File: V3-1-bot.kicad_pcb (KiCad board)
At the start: 4 copper layers, 145 x 74.9 mm, 36 parts, among them IC1 MCP4451-103E_ST, IC2 MCP4451-103E_ST, IC3 MCP4451-103E_ST, J1 PowerPole, J2 Conn_01x12_Female, J3 Conn_01x12_Female, J4 Conn_01x03_Female, J5 Conn_01x03_Female, J6 Conn_01x03_Female, J7 Conn_01x03_Female, J8 Conn_01x03_Female, J9 Conn_01x03_Female, U1 Teensy4.0-Tall-Dog-Breakout, U2 AMPLIFIER-PAM8403, U3 AMPLIFIER-PAM8403, U4 AMPLIFIER-PAM8403, U5 AMPLIFIER-PAM8403, U6 AMPLIFIER-PAM8403, U7 AMPLIFIER-PAM8403

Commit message: Updated BOT
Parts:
- moved R1 112.8 mm to (38.6, 82.3), turned to 90 degrees
- moved R2 107.9 mm to (43.7, 82.3), turned to 90 degrees
- moved J2 95.4 mm to (35.3, 89.2), turned to 90 degrees
- moved J3 89.6 mm to (35.1, 96.3), turned to 90 degrees
- moved R12 25.1 mm to (105.4, 119.9)
- moved C1 17.6 mm to (43.2, 115.3)
- moved C2 17.2 mm to (124.5, 116.3)
- moved C3 17.0 mm to (83.6, 116.3)
- moved U1 16.6 mm to (89.7, 87.9)
- moved J4 16.3 mm to (165.9, 137.4)
- moved J5 15.3 mm to (108.7, 137.4)
- moved R9 15.1 mm to (139.2, 118.9), turned to 0 degrees
- moved R3 14.8 mm to (57.9, 119.1)
- moved J6 14.3 mm to (108.7, 107.4)
- moved J8 13.7 mm to (165.9, 107.4)
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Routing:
- net VDD: track 0.00 -> 273.9 mm
- net GND: track 0.00 -> 210.8 mm
- net SPEAK7-: track 0.00 -> 135.7 mm
- net SPEAK8-: track 0.00 -> 132.2 mm
- net SPEAK7+: track 0.00 -> 129.8 mm, vias 0 -> 1
- net SPEAK8+: track 0.00 -> 120.2 mm, vias 0 -> 1
- net SPEAK5-: track 0.00 -> 112.2 mm
- net SPEAK5+: track 0.00 -> 104.8 mm, vias 0 -> 1
- net SPEAK6+: track 0.00 -> 93.4 mm, vias 0 -> 1
- net SPEAK6-: track 0.00 -> 93.3 mm
- net SPEAK11-: track 0.00 -> 81.5 mm
- net SPEAK11+: track 0.00 -> 73.1 mm
- net SPEAK9-: track 0.00 -> 69.9 mm, vias 0 -> 1
- net FREQ14: track 0.00 -> 67.7 mm
- net SPEAK1-: track 0.00 -> 67.3 mm
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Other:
- board size 145 x 74.9 mm -> 145 x 71.4 mm

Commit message: Done BOT v3.1
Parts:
- added ?: , HART:hart-logo-2000-2000dpi, F.Cu at (41.7, 76.5)
- R1, R2: moved to B.Cu
- U1: footprint Teensy:TallDogTeensy4.0Breakout -> HART:TallDogTeensy4.0Breakout
- U2, U3, U4, U5, U6, U7: value AMPLIFIER-PAM8403 -> >VALUE
- moved R1 51.8 mm to (89.2, 93.8)
- moved R2 42.0 mm to (84.1, 93.8)
- moved R6 7.19 mm to (58.2, 123.4), turned to 0 degrees
- moved R3 6.12 mm to (51.8, 118.4), turned to 0 degrees
- moved R12 5.80 mm to (99.6, 120.1)
- moved R5 5.56 mm to (58.1, 118.4), turned to 0 degrees
- moved R4 2.36 mm to (51.8, 123.7), turned to 0 degrees
- moved R11 0.76 mm to (99.5, 123.3)
- moved R13 0.76 mm to (93.5, 123.3)
- moved R14 0.76 mm to (93.5, 119.9)
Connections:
- J5 pad 2: GND -> (no net)
- R6 pad 1: (no net) -> FREQ1
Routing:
- net FREQ4: track 0.00 -> 165.1 mm, vias 0 -> 2
- net FREQ2: track 0.00 -> 163.9 mm, vias 0 -> 2
- net TeensyVDD: track 54.9 -> 218.2 mm, vias 3 -> 10
- net FREQ3: track 0.00 -> 160.9 mm, vias 0 -> 2
- net FREQ10: track 0.00 -> 158.6 mm, vias 0 -> 1
- net FREQ1: track 0.00 -> 156.4 mm, vias 0 -> 2
- net FREQ9: track 0.00 -> 138.9 mm, vias 0 -> 2
- net SCL0: track 2.95 -> 122.7 mm, vias 1 -> 5
- net SDA0: track 2.08 -> 120.3 mm, vias 1 -> 5
- net FREQ8: track 0.00 -> 101.0 mm, vias 0 -> 2
- net FREQ13: track 0.00 -> 98.7 mm
- net FREQ6: track 1.80 -> 100.3 mm, vias 1 -> 2
- net GND: track 210.8 -> 308.8 mm
- net FREQ7: track 0.00 -> 92.2 mm, vias 0 -> 2
- net FREQ5: track 1.73 -> 89.4 mm, vias 1 -> 2
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- added copper zone on B.Cu, net GND
- added copper zone on F.Cu, net TeensyVDD
- added copper zone on F.Cu, net VDD
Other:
- outline, holes or cut-outs redrawn
- board text added: "GND"
- board text added: "HART Prototype V3.1"
- board text added: "VDD"
- board text added: "WARNING! DO NOT REVERSE POLARITY!!"

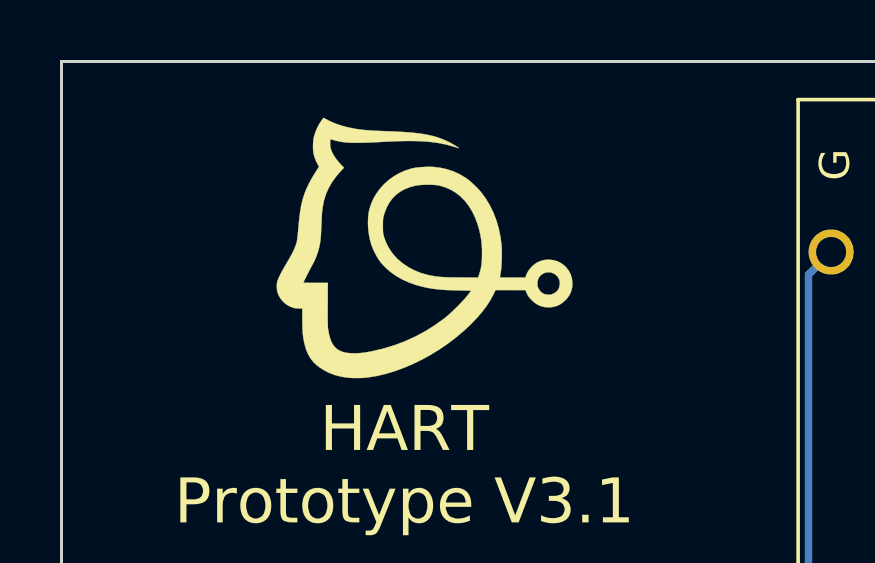
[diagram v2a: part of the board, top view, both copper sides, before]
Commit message: Cleanup symbols and libraries and add separate submodule for kicad-libaries
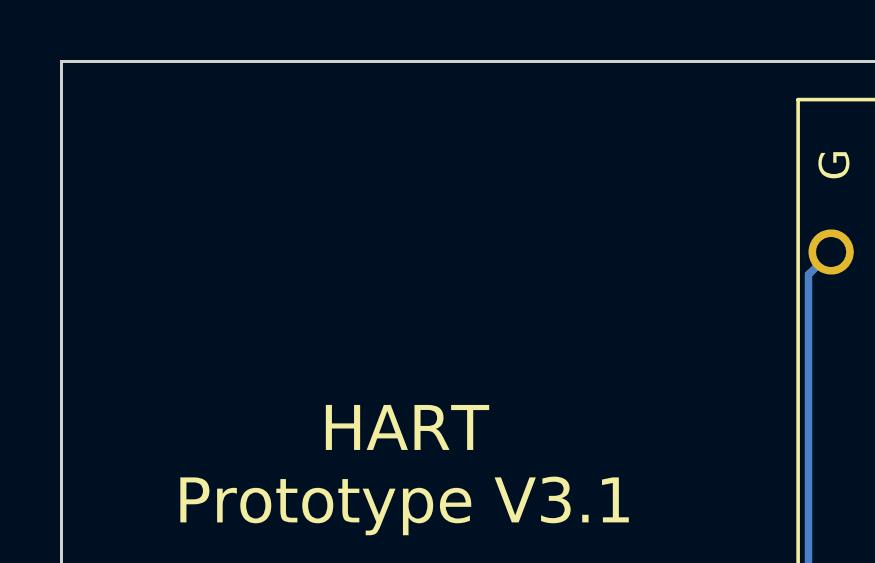
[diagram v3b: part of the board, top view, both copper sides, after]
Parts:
- removed ?: , HART:hart-logo-2000-2000dpi
- U2, U3, U4, U5, U6, U7: value >VALUE -> AMPLIFIER-PAM8403
